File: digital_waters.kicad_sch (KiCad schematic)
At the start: 12 parts, among them J12 SLOT 2, J13 SLOT 1

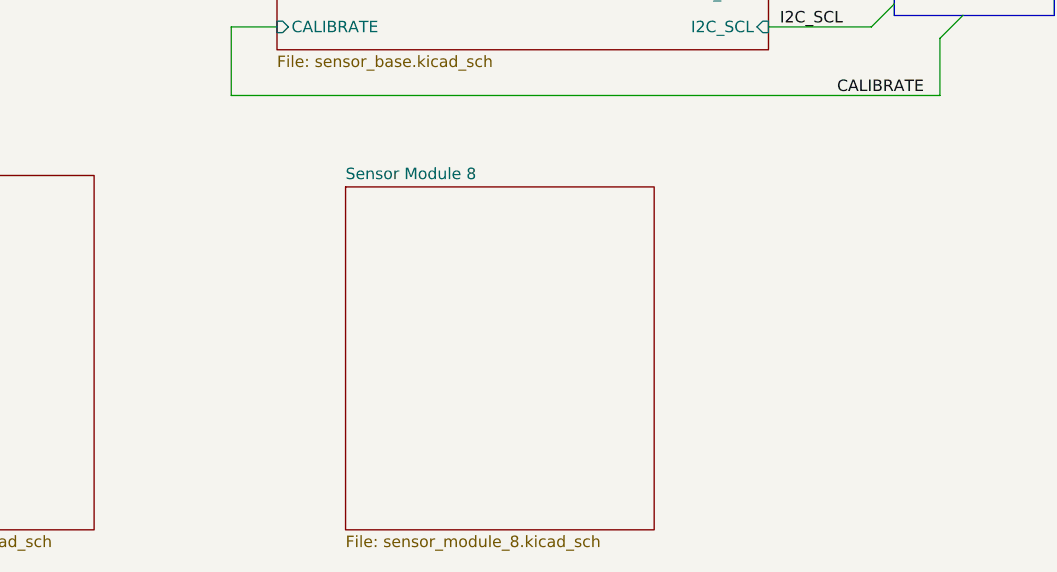
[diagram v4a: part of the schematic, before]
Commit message: Added some notes to otherwise blank pages. Added the full 8 sensor buffers to the 8 sensor analog board. Added a decoupling sub page to same. Changed a couple of sensor labels on base and 4 board just as placeholders
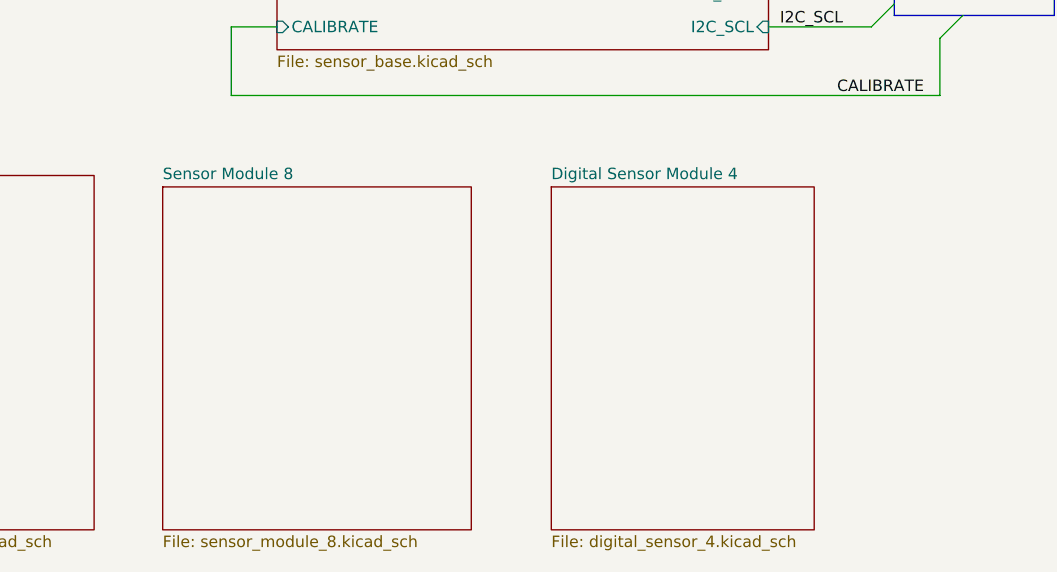
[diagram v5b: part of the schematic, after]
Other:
- added sheet Digital Sensor Module 4 (digital_sensor_4.kicad_sch)
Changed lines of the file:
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@@
 	)
 	(sheet
-		(at 91.44 129.54)
+		(at 71.12 129.54)
 		(size 34.29 38.1)
 		(fields_autoplaced yes)
@@
 		)
 		(property "Sheetname" "Sensor Module 8"
-			(at 91.44 128.8284 0)
+			(at 71.12 128.8284 0)
 			(effects
 				(font
@@
 		)
 		(property "Sheetfile" "sensor_module_8.kicad_sch"
-			(at 91.44 168.2246 0)
+			(at 71.12 168.2246 0)
 			(effects
 				(font
@@
 				)
 			)
+		)
+	)
+	(sheet
+		(at 114.3 129.54)
+		(size 29.21 38.1)
+		(fields_autoplaced yes)
+		(stroke
+			(width 0.1524)
+			(type solid)
+		)
+		(fill
+			(color 0 0 0 0.0000)
+		)
+		(property "Sheetname" "Digital Sensor Module 4"
+			(at 114.3 128.8284 0)
+			(effects
+				(font
+					(size 1.27 1.27)
+				)
+				(justify left bottom)
+			)
+		)
+		(property "Sheetfile" "digital_sensor_4.kicad_sch"
+			(at 114.3 168.2246 0)
+			(effects
+				(font
+					(size 1.27 1.27)
+				)
+				(justify left top)
+			)
+		)
+		(instances
+			(project "digital_waters"
+				(path "/37fdfe07-1a70-41c8-8af2-e03e19737580"
+					(page "7")
+				)
+			)

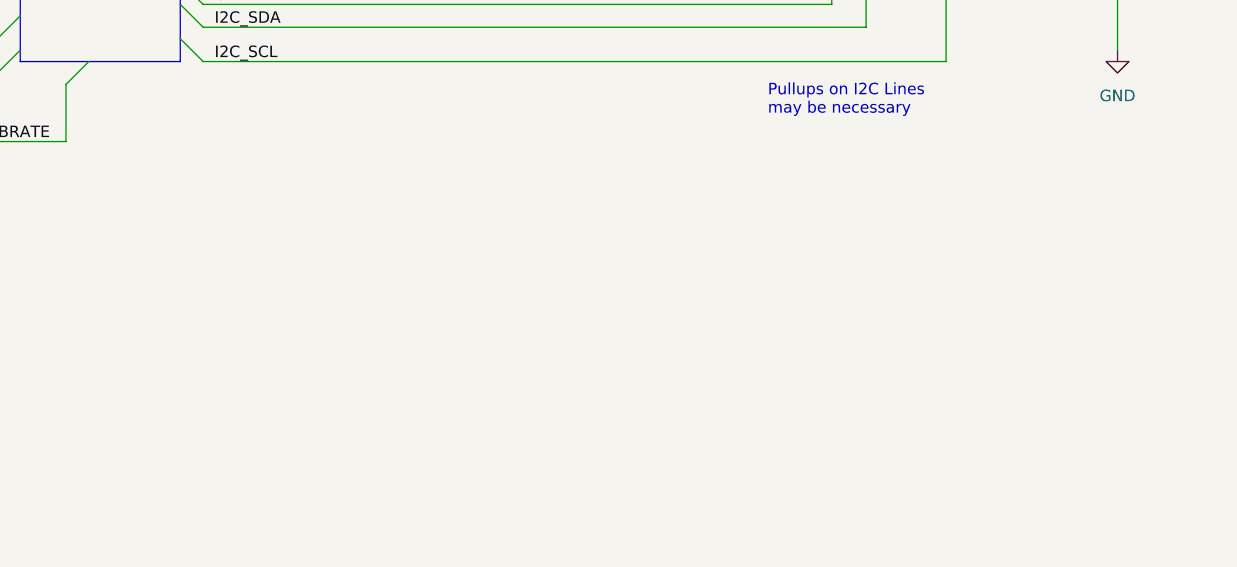
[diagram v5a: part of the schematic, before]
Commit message: Oopsie. - Changed Channel 7 on the analog 8 board to a calibration input. - Added a TODO to the root page
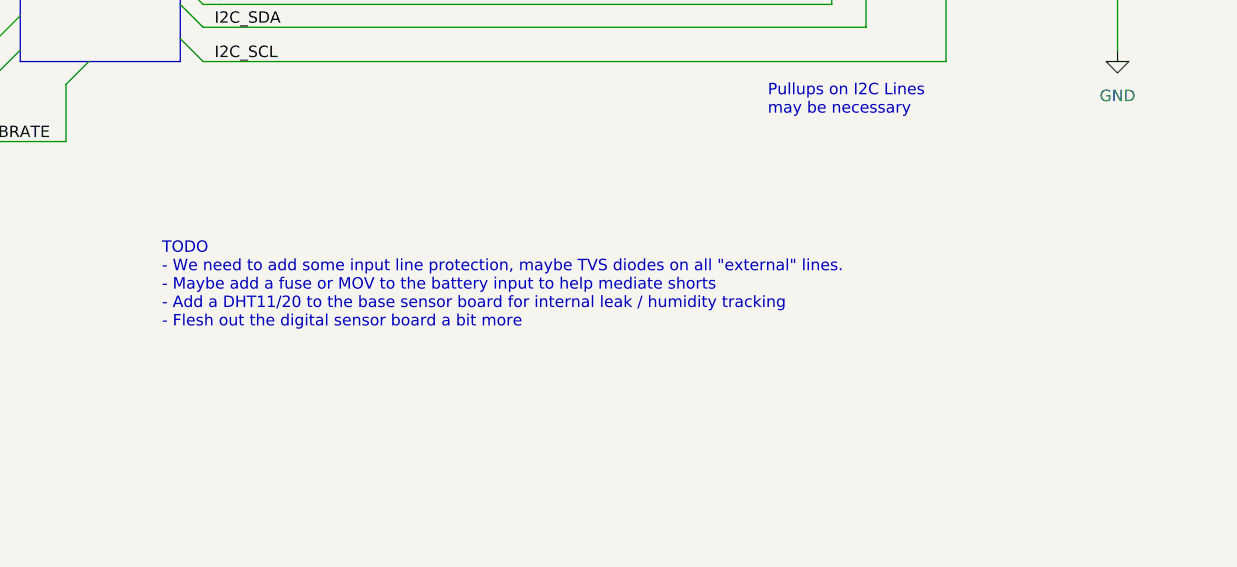
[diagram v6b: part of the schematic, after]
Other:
- note added: "TODO - We need to add some input line protection, maybe TVS diodes on all "external" lines. - Maybe add a fuse or MOV to the battery input to help mediate shorts - Add a DHT11/20 to the base sensor board for internal leak / humidity tracking - Flesh out the digital sensor board a bit more"
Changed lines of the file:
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@@
+		)
+	)
+	(text "TODO\n- We need to add some input line protection, maybe TVS diodes on all \"external\" lines.\n- Maybe add a fuse or MOV to the battery input to help mediate shorts\n- Add a DHT11/20 to the base sensor board for internal leak / humidity tracking\n- Flesh out the digital sensor board a bit more\n"
+		(exclude_from_sim no)
+		(at 168.148 135.382 0)
+		(effects
+			(font
+				(size 1.27 1.27)
+			)
+			(justify left)
 		)
 	)

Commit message: Updated the ORP and pH probes with a more appropriate amp. Added some notes. Added a tentative PL-100 adapter circuit. Added Vref buffering. Started move towards ESP32 ADC converter for base sensors.
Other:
- sheet Micocontroller ports: added 1_WIRE_SDA, ADC_BATT+, ADC_BATT-, ADC_TEMP; removed none
- note added: "Notes: INA333 requires that signals be at least 0.1V away from the power rails, both ground and VDD. Input signals must be at least 100mV above ground! There is a 70pA input offset current which also must have a path to ground. Inputs should provide this path through a resistor or balanced resistors."
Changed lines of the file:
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@@
+		)
+	)
+	(text "Notes:\nINA333 requires that signals be at least 0.1V away from the \npower rails, both ground and VDD. Input signals must be\nat least 100mV above ground!\nThere is a 70pA input offset current which also must have\na path to ground. Inputs should provide this path through \na resistor or balanced resistors. "
+		(exclude_from_sim no)
+		(at 164.592 142.494 0)
+		(effects
+			(font
+				(size 1.27 1.27)
+			)
+			(justify left)
 		)
 	)
 	(text "TODO\n- We need to add some input line protection, maybe TVS diodes on all \"external\" lines.\n- Maybe add a fuse or MOV to the battery input to help mediate shorts\n- Add a DHT11/20 to the base sensor board for internal leak / humidity tracking\n- Flesh out the digital sensor board a bit more\n"
 		(exclude_from_sim no)
-		(at 168.148 135.382 0)
+		(at 164.338 128.27 0)
 		(effects
 			(font
@@
 	(text "General Design requirements:\n- Power switching (need to be able to reduce power consumption \n  as much as possible). Everything that draws power must be able \n  to be switched off or must have a shutdown pin.\n- Low noise interfaces on sensor inputs.\n- High frequency lines should be adequately blocked"
 		(exclude_from_sim no)
-		(at 10.414 0.254 0)
+		(at 165.354 158.242 0)
 		(effects
 			(font
@@
 			)
 		)
+		(pin "ADC_TEMP" input
+			(at 83.82 53.34 180)
+			(effects
+				(font
+					(size 1.27 1.27)
+				)
+				(justify left)
+			)
+		)
+		(pin "ADC_BATT+" input
+			(at 83.82 57.15 180)
+			(effects
+				(font
+					(size 1.27 1.27)
+				)
+				(justify left)
+			)
+		)
+		(pin "ADC_BATT-" input
+			(at 83.82 60.96 180)
+			(effects
+				(font
+					(size 1.27 1.27)
+				)
+				(justify left)
+			)
+		)
+		(pin "1_WIRE_SDA" output
+			(at 83.82 67.31 180)
+			(effects
+				(font
+					(size 1.27 1.27)
+				)
+				(justify left)
+			)
+		)

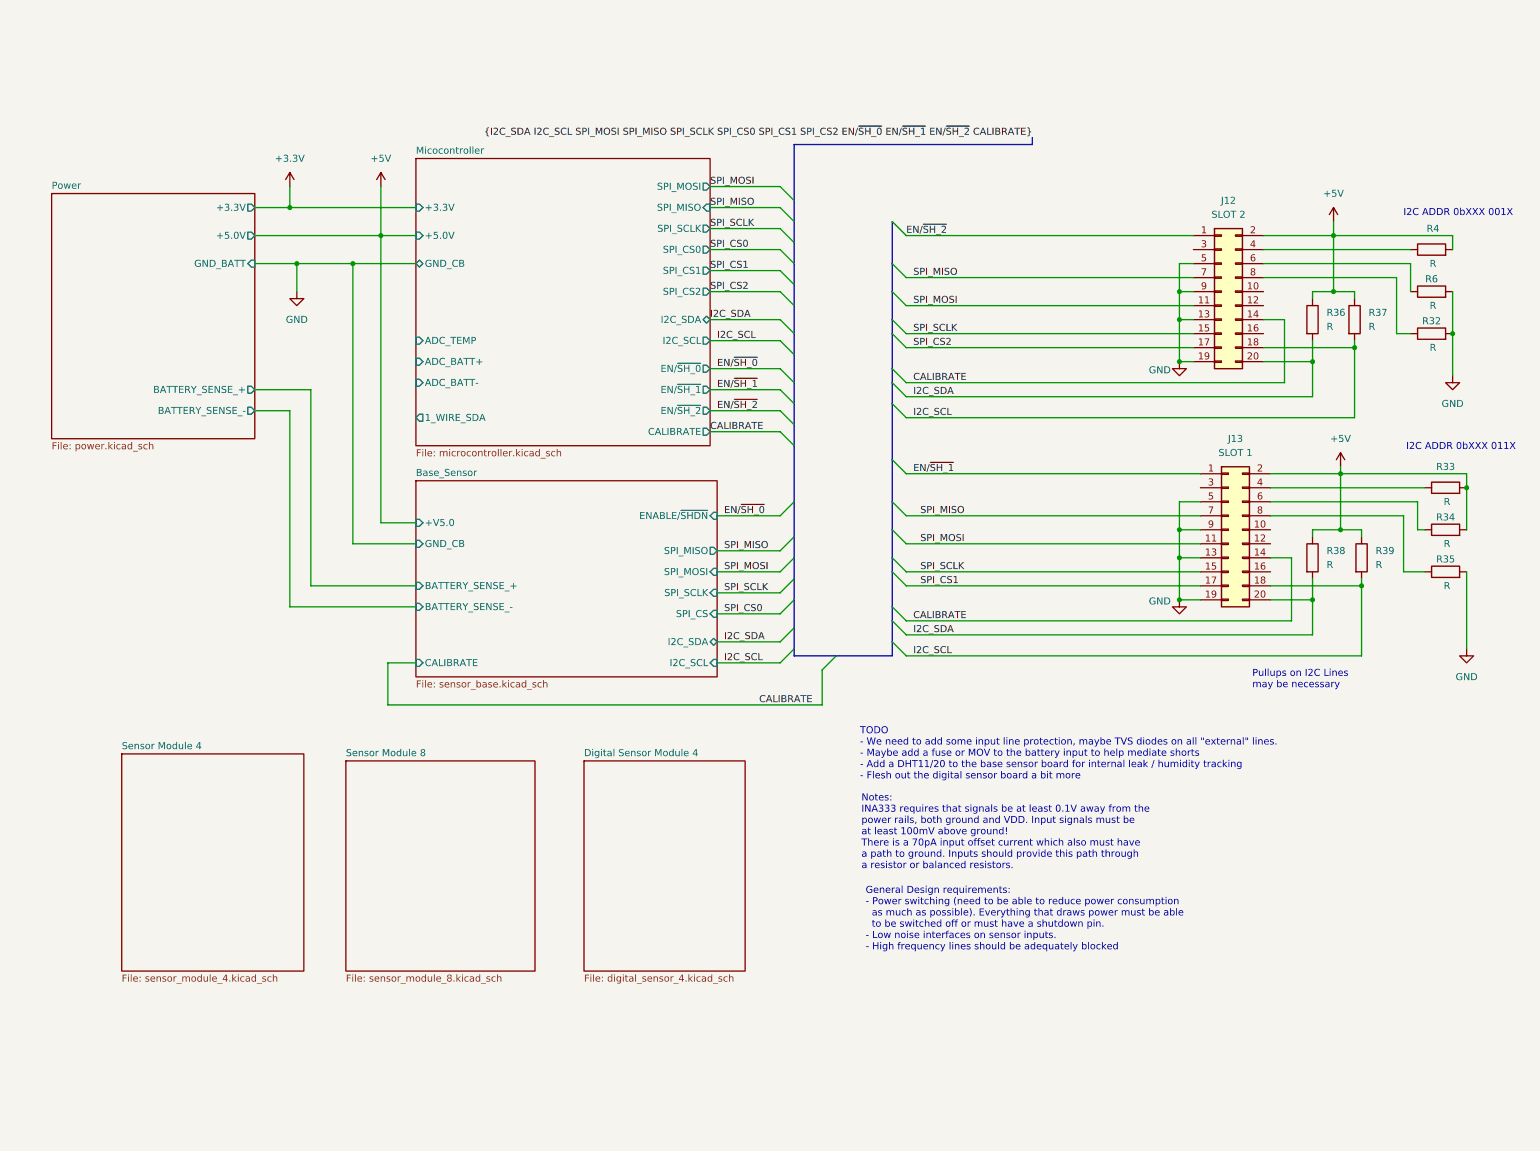
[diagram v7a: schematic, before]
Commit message: Cleaned up a bit Added a SPDT to calibrate signal on the base board Added PTC and MOV to power section
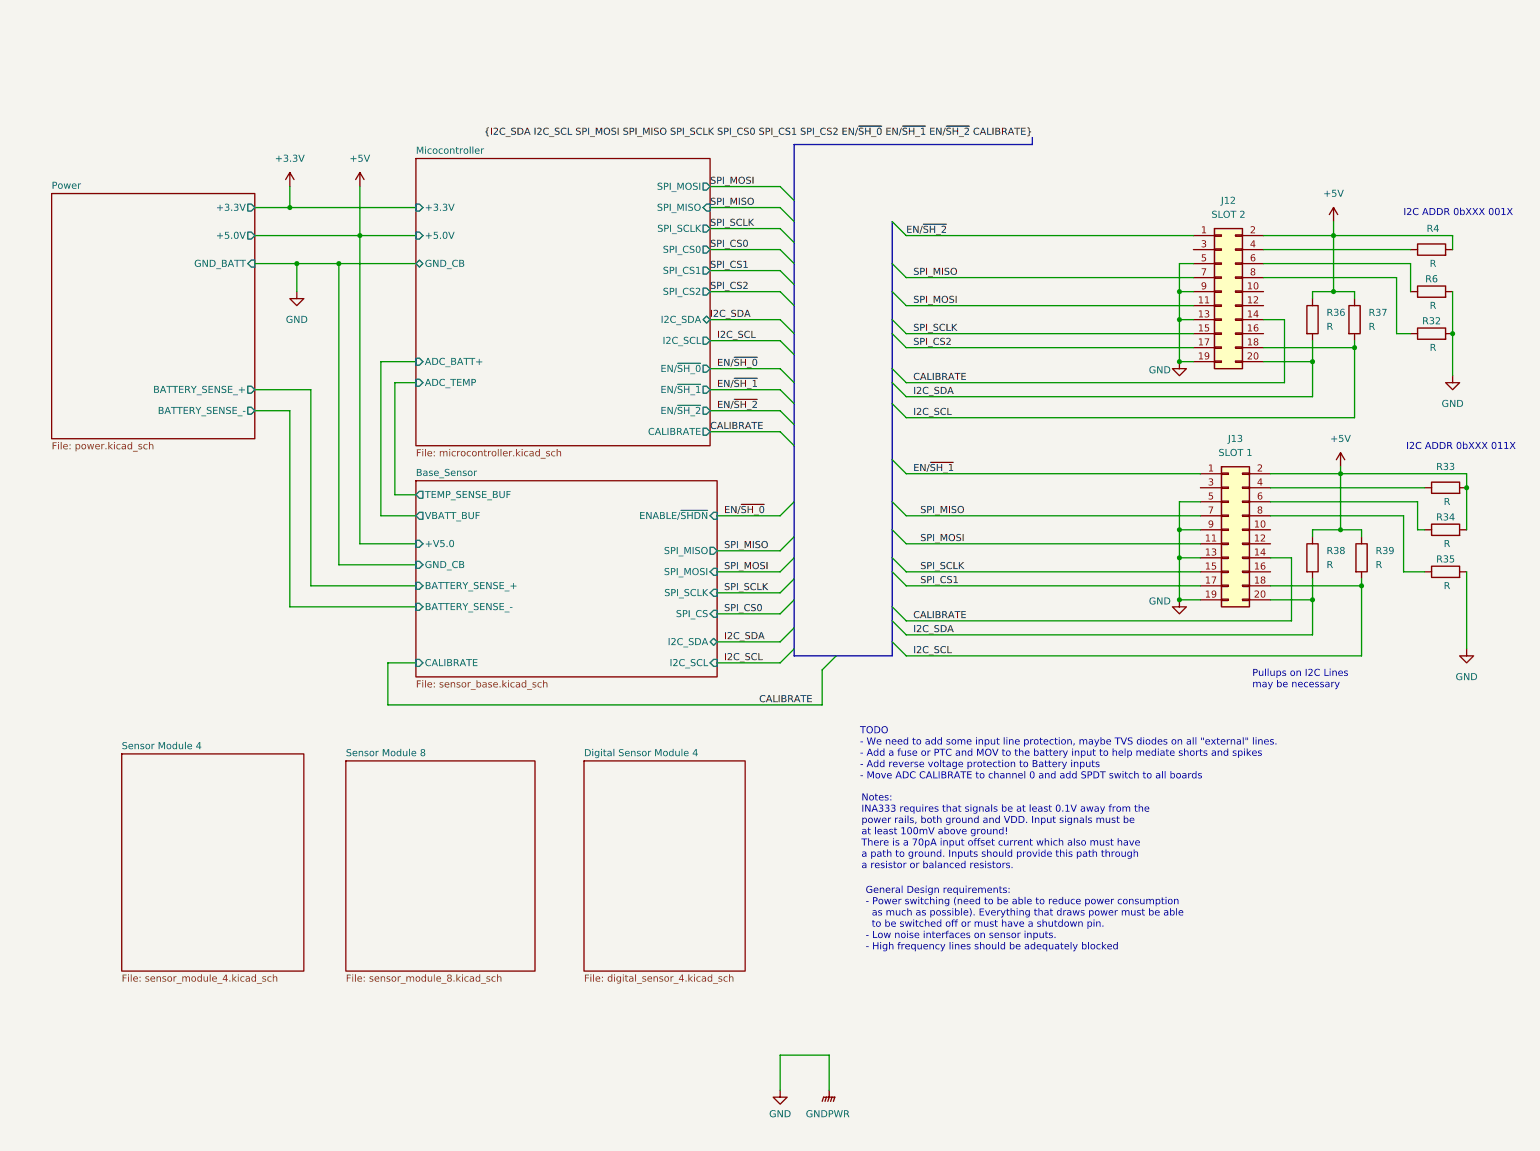
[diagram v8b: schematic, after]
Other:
- sheet Base_Sensor ports: added TEMP_SENSE_BUF, VBATT_BUF; removed none
- sheet Micocontroller ports: added none; removed 1_WIRE_SDA, ADC_BATT-
- note added: "TODO - We need to add some input line protection, maybe TVS diodes on all "external" lines. - Add a fuse or PTC and MOV to the battery input to help mediate shorts and spikes - Add reverse voltage protection to Battery inputs - Move ADC CALIBRATE to channel 0 and add SPDT switch to all boards"
- note removed: "TODO - We need to add some input line protection, maybe TVS diodes on all "external" lines. - Maybe add a fuse or MOV to the battery input to help mediate shorts - Add a DHT11/20 to the base sensor board for internal leak / humidity tracking - Flesh out the digital sensor board a bit more"
